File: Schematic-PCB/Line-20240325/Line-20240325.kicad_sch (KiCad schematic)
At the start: 164 parts, among them J1 Conn_01x02_Pin, J2 Conn_01x04_Pin, J3 Conn_01x06_Pin, SW1 SW_Push, U33 ATmega2560-16A, Y1 16MHz

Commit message: ラインセンサの配線を進めた
マジキツイ
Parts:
- C1: footprint Capacitor_SMD:C_0603_1608Metric -> Capacitor_THT:CP_Radial_D10.0mm_P5.00mm
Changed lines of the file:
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@@
 			)
 		)
-		(property "Footprint" "Capacitor_SMD:C_0603_1608Metric"
+		(property "Footprint" "Capacitor_THT:CP_Radial_D10.0mm_P5.00mm"
 			(at 74.6252 325.12 0)
 			(effects

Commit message: CNCとか3Dプリンタとか基板とかいろいろ編集したよ
進捗生んでる...?
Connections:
- net GND: now also J3.1 (Pin_1); no longer J3.6 (Pin_6)
- net RX-USB: now also J3.5 (Pin_5); no longer J3.2 (Pin_2)
- net TX-USB: now also J3.4 (Pin_4); no longer J3.3 (Pin_3)
- net at C8.1: now also J3.6 (Pin_6); no longer J3.1 (Pin_1)
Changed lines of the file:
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@@
 	(symbol
 		(lib_id "Connector:Conn_01x06_Pin")
-		(at 375.92 273.05 0)
+		(at 375.92 275.59 0)
+		(mirror x)
 		(unit 1)
 		(exclude_from_sim no)
@@
 		(on_board yes)
 		(dnp no)
-		(fields_autoplaced yes)
 		(property "Reference" "J3"
-			(at 376.555 262.89 0)
+			(at 376.555 285.75 0)
 			(effects
 				(font
@@
 		)
 		(property "Value" "Conn_01x06_Pin"
-			(at 376.555 265.43 0)
+			(at 376.555 283.21 0)
 			(effects
 				(font
@@
 		)
 		(property "Footprint" "Connector_PinSocket_2.54mm:PinSocket_1x06_P2.54mm_Horizontal"
-			(at 375.92 273.05 0)
+			(at 375.92 275.59 0)
 			(effects
 				(font
@@
 		)
 		(property "Datasheet" "~"
-			(at 375.92 273.05 0)
+			(at 375.92 275.59 0)
 			(effects
 				(font
@@
 		)
 		(property "Description" "Generic connector, single row, 01x06, script generated"
-			(at 375.92 273.05 0)
+			(at 375.92 275.59 0)
 			(effects
 				(font

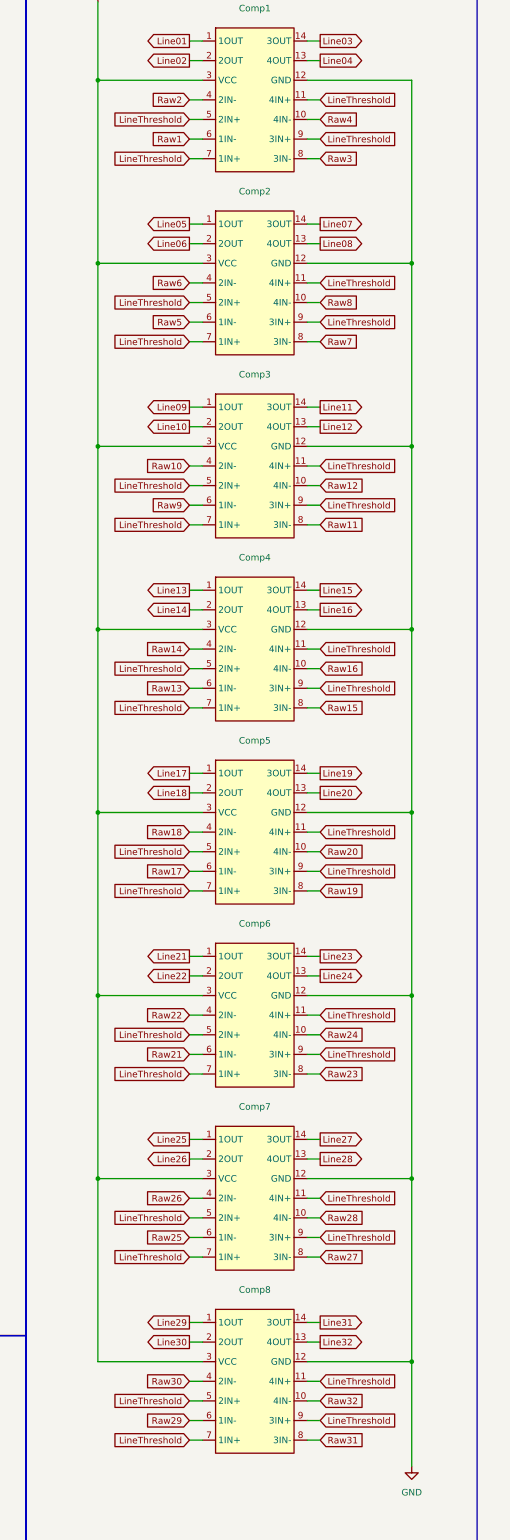
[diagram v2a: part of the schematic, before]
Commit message: ライン基板の配線を直した
IN- に line_threshold を繋ぐように変更した
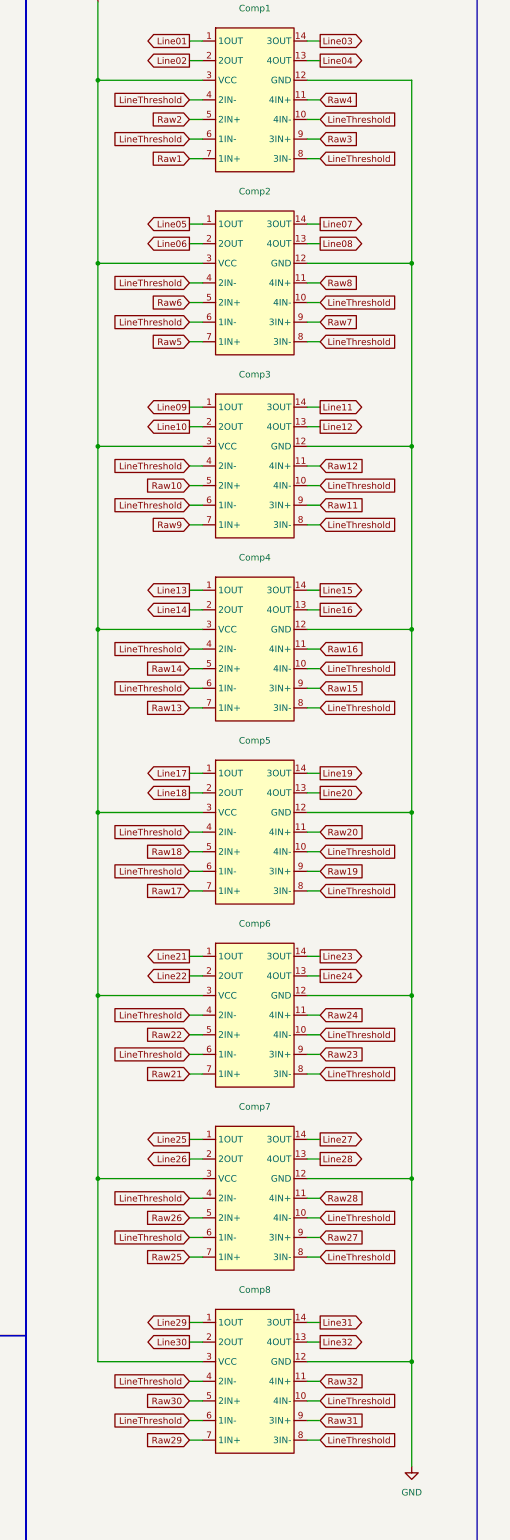
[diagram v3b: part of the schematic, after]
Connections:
- net LineThreshold: now also Comp1.10 (4IN-), Comp1.4 (2IN-), Comp1.6 (1IN-), Comp1.8 (3IN-), Comp2.10 (4IN-), Comp2.4 (2IN-), Comp2.6 (1IN-), Comp2.8 (3IN-), Comp3.10 (4IN-), Comp3.4 (2IN-), Comp3.6 (1IN-), Comp3.8 (3IN-), Comp4.10 (4IN-), Comp4.4 (2IN-), Comp4.6 (1IN-), Comp4.8 (3IN-), Comp5.10 (4IN-), Comp5.4 (2IN-), Comp5.6 (1IN-), Comp5.8 (3IN-), Comp6.10 (4IN-), Comp6.4 (2IN-), Comp6.6 (1IN-), Comp6.8 (3IN-), Comp7.10 (4IN-), Comp7.4 (2IN-), Comp7.6 (1IN-), Comp7.8 (3IN-), Comp8.10 (4IN-), Comp8.4 (2IN-), Comp8.6 (1IN-), Comp8.8 (3IN-); no longer Comp1.11 (4IN+), Comp1.5 (2IN+), Comp1.7 (1IN+), Comp1.9 (3IN+), Comp2.11 (4IN+), Comp2.5 (2IN+), Comp2.7 (1IN+), Comp2.9 (3IN+), Comp3.11 (4IN+), Comp3.5 (2IN+), Comp3.7 (1IN+), Comp3.9 (3IN+), Comp4.11 (4IN+), Comp4.5 (2IN+), Comp4.7 (1IN+), Comp4.9 (3IN+), Comp5.11 (4IN+), Comp5.5 (2IN+), Comp5.7 (1IN+), Comp5.9 (3IN+), Comp6.11 (4IN+), Comp6.5 (2IN+), Comp6.7 (1IN+), Comp6.9 (3IN+), Comp7.11 (4IN+), Comp7.5 (2IN+), Comp7.7 (1IN+), Comp7.9 (3IN+), Comp8.11 (4IN+), Comp8.5 (2IN+), Comp8.7 (1IN+), Comp8.9 (3IN+)
- net Raw1: now also Comp1.7 (1IN+); no longer Comp1.6 (1IN-)
- net Raw10: now also Comp3.5 (2IN+); no longer Comp3.4 (2IN-)
- net Raw11: now also Comp3.9 (3IN+); no longer Comp3.8 (3IN-)
- net Raw12: now also Comp3.11 (4IN+); no longer Comp3.10 (4IN-)
- net Raw13: now also Comp4.7 (1IN+); no longer Comp4.6 (1IN-)
- net Raw14: now also Comp4.5 (2IN+); no longer Comp4.4 (2IN-)
- net Raw15: now also Comp4.9 (3IN+); no longer Comp4.8 (3IN-)
- net Raw16: now also Comp4.11 (4IN+); no longer Comp4.10 (4IN-)
- net Raw17: now also Comp5.7 (1IN+); no longer Comp5.6 (1IN-)
- net Raw18: now also Comp5.5 (2IN+); no longer Comp5.4 (2IN-)
- net Raw19: now also Comp5.9 (3IN+); no longer Comp5.8 (3IN-)
- net Raw2: now also Comp1.5 (2IN+); no longer Comp1.4 (2IN-)
- net Raw20: now also Comp5.11 (4IN+); no longer Comp5.10 (4IN-)
- net Raw21: now also Comp6.7 (1IN+); no longer Comp6.6 (1IN-)
- net Raw22: now also Comp6.5 (2IN+); no longer Comp6.4 (2IN-)
- net Raw23: now also Comp6.9 (3IN+); no longer Comp6.8 (3IN-)
- net Raw24: now also Comp6.11 (4IN+); no longer Comp6.10 (4IN-)
- net Raw25: now also Comp7.7 (1IN+); no longer Comp7.6 (1IN-)
- net Raw26: now also Comp7.5 (2IN+); no longer Comp7.4 (2IN-)
- net Raw27: now also Comp7.9 (3IN+); no longer Comp7.8 (3IN-)
- net Raw28: now also Comp7.11 (4IN+); no longer Comp7.10 (4IN-)
- net Raw29: now also Comp8.7 (1IN+); no longer Comp8.6 (1IN-)
- net Raw3: now also Comp1.9 (3IN+); no longer Comp1.8 (3IN-)
- net Raw30: now also Comp8.5 (2IN+); no longer Comp8.4 (2IN-)
- net Raw31: now also Comp8.9 (3IN+); no longer Comp8.8 (3IN-)
- net Raw32: now also Comp8.11 (4IN+); no longer Comp8.10 (4IN-)
- net Raw4: now also Comp1.11 (4IN+); no longer Comp1.10 (4IN-)
- net Raw5: now also Comp2.7 (1IN+); no longer Comp2.6 (1IN-)
- net Raw6: now also Comp2.5 (2IN+); no longer Comp2.4 (2IN-)
- net Raw7: now also Comp2.9 (3IN+); no longer Comp2.8 (3IN-)
- net Raw8: now also Comp2.11 (4IN+); no longer Comp2.10 (4IN-)
- net Raw9: now also Comp3.7 (1IN+); no longer Comp3.6 (1IN-)

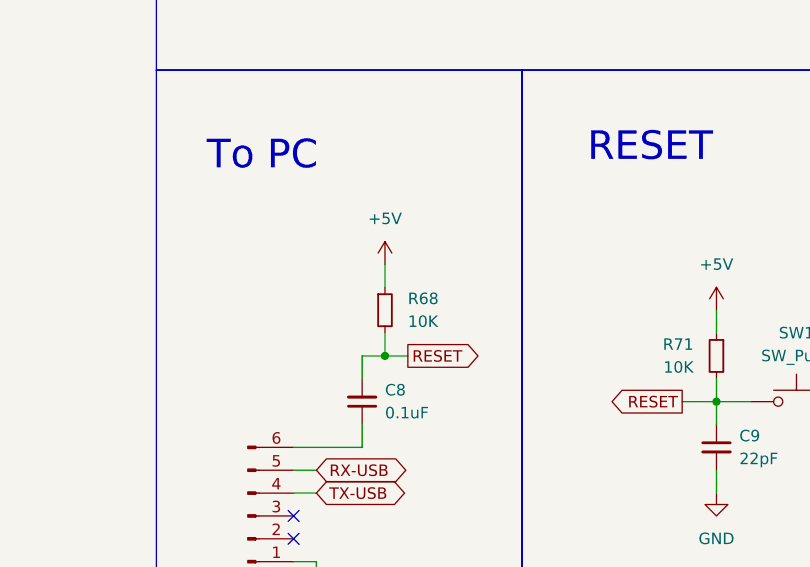
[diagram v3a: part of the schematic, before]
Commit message: ラインセンサ基板の配線をちょっと進めた
CPUとかの配置を変更したよ
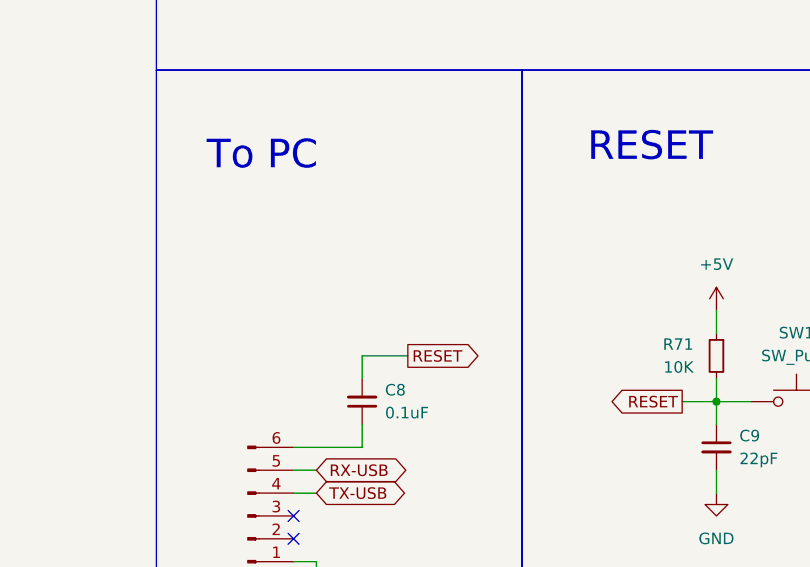
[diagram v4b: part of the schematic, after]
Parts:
- removed R68: 10K, Resistor_SMD:R_0603_1608Metric, symbol Device:R_Small
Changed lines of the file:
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@@
 	)
 	(junction
-		(at 391.16 257.81)
-		(diameter 0)
-		(color 0 0 0 0)
-	)
-	(junction
 		(at 229.87 125.73)
 		(diameter 0)
@@
 	(wire
 		(pts
-			(xy 391.16 255.27) (xy 391.16 257.81)
-		)
-		(stroke
-			(width 0)
-			(type default)
-		)
-	)
-	(wire
-		(pts
 			(xy 85.09 218.44) (xy 87.63 218.44)
 		)
@@
 	(wire
 		(pts
-			(xy 391.16 247.65) (xy 391.16 250.19)
-		)
-		(stroke
-			(width 0)
-			(type default)
-		)
-	)
-	(wire
-		(pts
 			(xy 74.93 193.04) (xy 77.47 193.04)
 		)
@@
 	(wire
 		(pts
-			(xy 391.16 257.81) (xy 393.7 257.81)
-		)
-		(stroke
-			(width 0)
-			(type default)
-		)
-	)
-	(wire
-		(pts
 			(xy 381 273.05) (xy 383.54 273.05)
 		)
@@
 	(wire
 		(pts
-			(xy 388.62 257.81) (xy 391.16 257.81)
+			(xy 388.62 257.81) (xy 393.7 257.81)
 		)
 		(stroke
@@
 	)
 	(symbol
-		(lib_id "Device:R_Small")
-		(at 391.16 252.73 0)
-		(unit 1)
-		(exclude_from_sim no)
-		(in_bom yes)
-		(on_board yes)
-		(dnp no)
-		(fields_autoplaced yes)
-		(property "Reference" "R68"
-			(at 393.7 251.46 0)
-			(effects
-				(font
-					(size 1.27 1.27)
-				)
-				(justify left)
-			)
-		)
-		(property "Value" "10K"
-			(at 393.7 254 0)
-			(effects
-				(font
-					(size 1.27 1.27)
-				)
-				(justify left)
-			)
-		)
-		(property "Footprint" "Resistor_SMD:R_0603_1608Metric"
-			(at 391.16 252.73 0)
-			(effects
-				(font
-					(size 1.27 1.27)
-				)
-				(hide yes)
-			)
-		)
-		(property "Datasheet" "~"
-			(at 391.16 252.73 0)
-			(effects
-				(font
-					(size 1.27 1.27)
-				)
-				(hide yes)
-			)
-		)
-		(property "Description" "Resistor, small symbol"
-			(at 391.16 252.73 0)
-			(effects
-				(font
-					(size 1.27 1.27)
-				)
-				(hide yes)
-			)
-		)
-		(pin "2"
-		)
-		(pin "1"
-		)
-		(instances
-			(project "Line-20240325"
-				(path "/3ba7fdd5-fa74-4790-8511-1df233340313"
-					(reference "R68")
-					(unit 1)
-				)
-			)
-		)
-	)
-	(symbol
 		(lib_id "Device:LED_Small")
 		(at 22.86 204.47 0)
@@
 					(unit 1)
 				)
-			)
-		)
-	)
-	(symbol
-		(lib_id "power:+5V")
-		(at 391.16 247.65 0)
-		(unit 1)
-		(exclude_from_sim no)
-		(in_bom yes)
-		(on_board yes)
-		(dnp no)
-		(fields_autoplaced yes)
-		(property "Reference" "#PWR052"
-			(at 391.16 251.46 0)
-			(effects
-				(font
-					(size 1.27 1.27)
-				)
-				(hide yes)
-			)
-		)
-		(property "Value" "+5V"
-			(at 391.16 242.57 0)
-			(effects
-				(font
-					(size 1.27 1.27)
-				)
-			)
-		)
-		(property "Footprint" ""
-			(at 391.16 247.65 0)
-			(effects
-				(font
-					(size 1.27 1.27)
-				)
-				(hide yes)
-			)
-		)
-		(property "Datasheet" ""
-			(at 391.16 247.65 0)
-			(effects
-				(font
-					(size 1.27 1.27)
-				)
-				(hide yes)
-			)
-		)
-		(property "Description" "Power symbol creates a global label with name \"+5V\""
-			(at 391.16 247.65 0)
-			(effects
-				(font
-					(size 1.27 1.27)
-				)
-				(hide yes)
-			)
-		)
-		(pin "1"
-		)
-		(instances
-			(project "Line-20240325"
-				(path "/3ba7fdd5-fa74-4790-8511-1df233340313"
-					(reference "#PWR052")
-					(unit 1)
-				)

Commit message: ライン回路修正
とりあえずICSPつけた
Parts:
- added J4: ICSP, symbol Connector_Generic:Conn_02x03_Odd_Even
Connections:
- net +5V: now also J4.2 (Pin_2)
- net GND: now also J4.6 (Pin_6)
- net RESET: now also J4.5 (Pin_5)
- net Line09 renamed Line09_SS
- net Line10 renamed Line10_SCK
- net Line10_SCK: now also J4.3 (Pin_3)
- net Line11 renamed Line11MOSI
- net Line11MOSI: no longer U33.21 (PB2/D51/MOSI)
- net Line12 renamed Line12_MISO
- net Line12_MISO: now also J4.1 (Pin_1)
- new net Line11_MOSI: J4.4 (Pin_4), U33.21 (PB2/D51/MOSI)
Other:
- note added: "ICSP"
- moved on the sheet: C8, C9, J3, R71, SW1

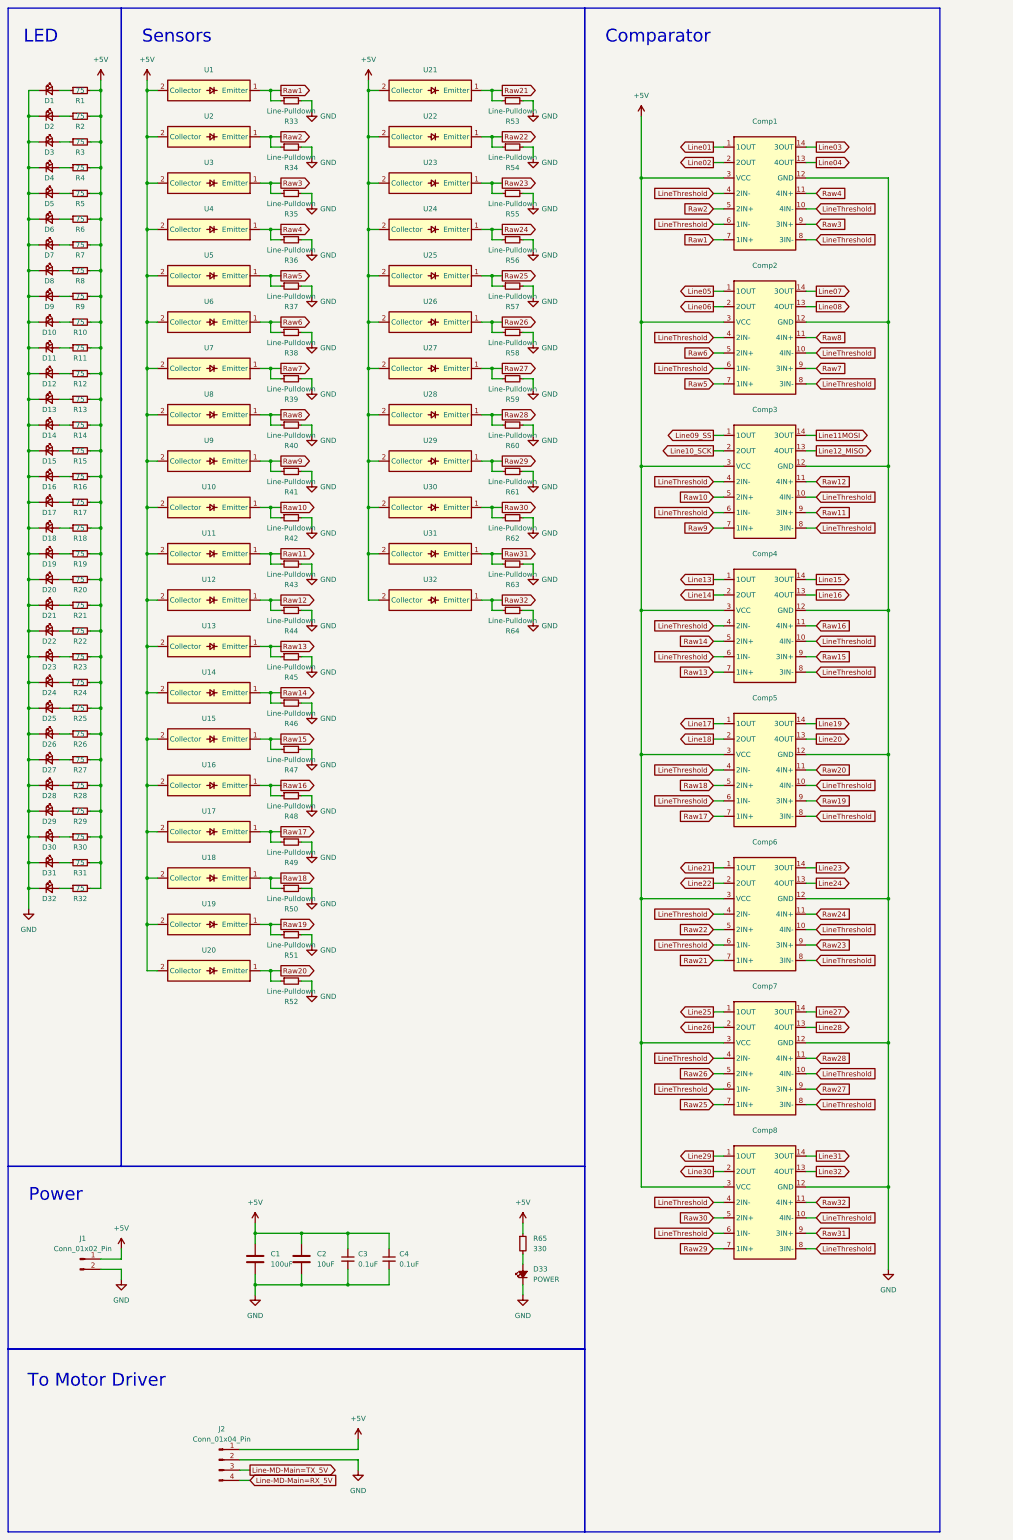
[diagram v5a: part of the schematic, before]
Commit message: update: ライン基板のLEDに電源オン/オフ用のスイッチを付けた
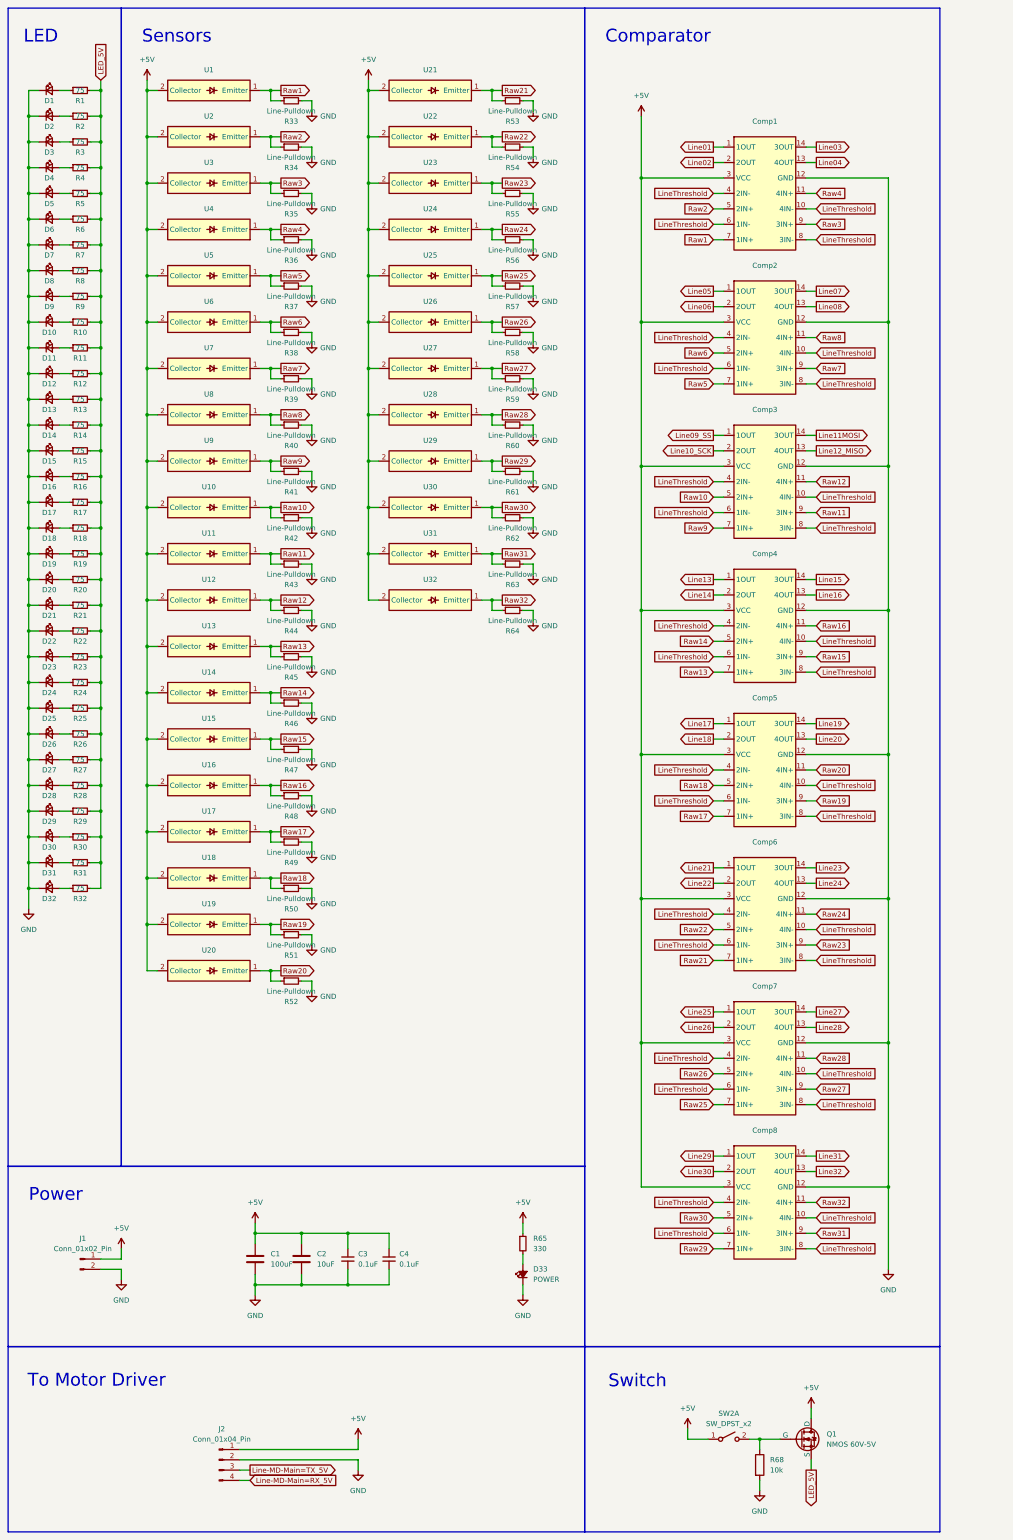
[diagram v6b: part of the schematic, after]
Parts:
- added Q1: NMOS 60V-5V, symbol Simulation_SPICE:NMOS
- added R68: 10k, symbol Device:R
- added SW2: SW_DPST_x2, symbol Switch:SW_DPST_x2
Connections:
- net +5V: now also Q1.1 (D), SW2.1 (A); no longer R1.2, R10.2, R11.2, R12.2, R13.2, R14.2, R15.2, R16.2, R17.2, R18.2, R19.2, R2.2, R20.2, R21.2, R22.2, R23.2, R24.2, R25.2, R26.2, R27.2, R28.2, R29.2, R3.2, R30.2, R31.2, R32.2, R4.2, R5.2, R6.2, R7.2, R8.2, R9.2
- net GND: now also R68.2
- new net: Q1.2 (G), R68.1, SW2.2 (B)
- new net LED_5V: Q1.3 (S), R1.2, R10.2, R11.2, R12.2, R13.2, R14.2, R15.2, R16.2, R17.2, R18.2, R19.2, R2.2, R20.2, R21.2, R22.2, R23.2, R24.2, R25.2, R26.2, R27.2, R28.2, R29.2, R3.2, R30.2, R31.2, R32.2, R4.2, R5.2, R6.2, R7.2, R8.2, R9.2
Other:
- note added: "Switch"
